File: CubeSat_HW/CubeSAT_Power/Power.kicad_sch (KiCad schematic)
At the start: 12 parts, among them J1 USB_B_Micro, J2 Conn_01x02_Pin, J4 Conn_02x20_Odd_Even, Q1 AO3401A, Q2 AO3401A, U1 LM1117MP-5.0

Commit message: feat: Added new version for the Power Supply Board
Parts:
- removed Q2: AO3401A, Package_TO_SOT_SMD:SOT-23, symbol Transistor_FET:AO3401A
- added D1: 12V, Diode_SMD:D_SOD-123, symbol Device:D_Zener
- added Q2: IRLML2502, Package_TO_SOT_SMD:SOT-23, symbol Transistor_FET:IRLZ44N
- added R1: 10k, Resistor_SMD:R_0603_1608Metric, symbol Device:R
- added R2: 10R, Resistor_SMD:R_0603_1608Metric, symbol Device:R
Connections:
- net COMMAND: now also R2.1
- net GND: now also D1.2 (A), Q2.3 (S), R1.2
- net VOut: now also Q2.2 (D)
- new net: D1.1 (K), Q2.1 (G), R1.1, R2.2

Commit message: fix: Minor fixes to the Power Supply Board
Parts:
- removed D1: 12V, Diode_SMD:D_SOD-123, symbol Device:D_Zener
- removed Q2: IRLML2502, Package_TO_SOT_SMD:SOT-23, symbol Transistor_FET:IRLZ44N
- added J6: Conn_02x20_Odd_Even, symbol Connector_Generic:Conn_02x20_Odd_Even
- added Q2: 2N7002, Package_TO_SOT_SMD:SOT-23, symbol Transistor_FET:2N7002
- added Q3: IRLM2502, Package_TO_SOT_SMD:SOT-23, symbol Transistor_FET:AO3401A
- added R3, R4, R5: 100k, Resistor_SMD:R_0603_1608Metric, symbol Device:R
- R1: value 10k -> 1k
- R2: value 10R -> 100k
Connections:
- net COMMAND: now also R1.2; no longer R2.1
- net GND: now also R2.2, Q2.2 (S), R3.1, R4.1; no longer R1.2
- net at R1.1: now also R2.1, Q2.1 (G); no longer R2.2
- net at J1.2 (D-): now also R4.2
- net at J1.3 (D+): now also R3.2
- net VOut: no longer names the net of C2.1, U1.2 (VO)
- net VOut: now also Q3.2 (S), R5.2; no longer J1.1 (VBUS)
- new net: Q2.3 (D), Q3.1 (G), R5.1
- new net: J1.1 (VBUS), Q3.3 (D)
- no-connect marks 3 -> 1
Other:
- moved on the sheet: J1

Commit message: release: Added version II of PS project.
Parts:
- removed J1: USB_B_Micro, Connector_USB:USB_Micro-B_GCT_USB3076-30-A, symbol Connector:USB_B_Micro
- added J3: USB_A, Connector_USB:USB_A_CNCTech_1001-011-01101_Horizontal, symbol Connector:USB_A
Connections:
- net GND: now also J3.4 (GND), J3.5 (Shield)
- net at R4.2: now also J3.2 (D-)
- net at R3.2: now also J3.3 (D+)
- net at Q3.3 (D): now also J3.1 (VBUS)
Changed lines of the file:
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@@
   (junction (at 77.724 23.241) (diameter 0) (color 0 0 0 0)
   )
+  (junction (at 24.13 72.136) (diameter 0) (color 0 0 0 0)
+  )
   (junction (at 66.548 34.925) (diameter 0) (color 0 0 0 0)
   )
   (junction (at 74.93 72.898) (diameter 0) (color 0 0 0 0)
-  )
-  (junction (at 24.638 72.136) (diameter 0) (color 0 0 0 0)
   )
   (junction (at 56.515 23.114) (diameter 0) (color 0 0 0 0)
@@
     (stroke (width 0) (type default))
   )
+  (wire (pts (xy 23.114 72.136) (xy 24.13 72.136))
+    (stroke (width 0) (type default))
+  )
   (wire (pts (xy 56.515 34.925) (xy 66.548 34.925))
     (stroke (width 0) (type default))
   )
-  (wire (pts (xy 24.638 72.136) (xy 24.638 74.422))
-    (stroke (width 0) (type default))
-  )
   (wire (pts (xy 56.515 23.114) (xy 50.292 23.114))
     (stroke (width 0) (type default))
@@
     (stroke (width 0) (type default))
   )
-  (wire (pts (xy 39.243 64.516) (xy 33.401 64.516))
+  (wire (pts (xy 33.274 64.516) (xy 39.243 64.516))
     (stroke (width 0) (type default))
   )
@@
     (stroke (width 0) (type default))
   )
-  (wire (pts (xy 23.241 72.136) (xy 24.638 72.136))
-    (stroke (width 0) (type default))
-  )
   (wire (pts (xy 227.33 33.655) (xy 246.888 33.655))
     (stroke (width 0) (type default))
@@
     (stroke (width 0) (type default))
   )
-  (wire (pts (xy 43.561 61.976) (xy 33.401 61.976))
+  (wire (pts (xy 33.274 61.976) (xy 43.561 61.976))
     (stroke (width 0) (type default))
   )
@@
     (stroke (width 0) (type default))
   )
+  (wire (pts (xy 24.13 72.136) (xy 24.13 74.168))
+    (stroke (width 0) (type default))
+  )
+  (wire (pts (xy 24.13 72.136) (xy 25.654 72.136))
+    (stroke (width 0) (type default))
+  )
   (wire (pts (xy 84.455 66.167) (xy 93.091 66.167))
     (stroke (width 0) (type default))
@@
     (stroke (width 0) (type default))
   )
-  (wire (pts (xy 24.638 72.136) (xy 25.781 72.136))
-    (stroke (width 0) (type default))
-  )
   (wire (pts (xy 28.067 23.114) (xy 40.132 23.114))
     (stroke (width 0) (type default))
@@
     (stroke (width 0) (type default))
   )
-  (wire (pts (xy 33.401 56.896) (xy 79.375 56.896))
+  (wire (pts (xy 33.274 56.896) (xy 79.375 56.896))
     (stroke (width 0) (type default))
   )
@@
       (effects (font (size 1.27 1.27)) hide)
     )
-    (pin "2")
-    (pin "1")
+    (pin "1")
+    (pin "2")
     (instances
       (project "Power"
@@
       (effects (font (size 1.27 1.27)) hide)
     )
-    (pin "2")
-    (pin "1")
+    (pin "1")
+    (pin "2")
     (instances
       (project "Power"
@@
       (effects (font (size 1.27 1.27)) hide)
     )
-    (pin "2")
-    (pin "1")
+    (pin "1")
+    (pin "2")
     (instances
       (project "Power"
@@
       (effects (font (size 1.27 1.27)) (justify left) hide)
     )
+    (pin "1")
     (pin "2")
     (pin "3")
-    (pin "1")
     (instances
       (project "Power"
@@
       (effects (font (size 1.27 1.27)) hide)
     )
-    (pin "2")
-    (pin "1")
+    (pin "1")
+    (pin "2")
     (instances
       (project "Power"
@@
         (path "/ac9d7e28-4551-4313-b6f7-b1e4cd4b0a31"
           (reference "#PWR04") (unit 1)
+        )
+      )
+    )
+  )
+  (symbol (lib_id "Connector:USB_A") (at 25.654 61.976 0) (unit 1)
+    (in_bom yes) (on_board yes) (dnp no) (fields_autoplaced)
+    (property "Reference" "J3" (at 25.654 49.276 0)
+      (effects (font (size 1.27 1.27)))
+    )
+    (property "Value" "USB_A" (at 25.654 51.816 0)
+      (effects (font (size 1.27 1.27)))
+    )
+    (property "Footprint" "Connector_USB:USB_A_CNCTech_1001-011-01101_Horizontal" (at 29.464 63.246 0)
+      (effects (font (size 1.27 1.27)) hide)
+    )
+    (property "Datasheet" " ~" (at 29.464 63.246 0)
+      (effects (font (size 1.27 1.27)) hide)
+    )
+    (pin "1")
+    (pin "2")
+    (pin "3")
+    (pin "4")
+    (pin "5")
+    (instances
+      (project "Power"
+        (path "/ac9d7e28-4551-4313-b6f7-b1e4cd4b0a31"
+          (reference "J3") (unit 1)
         )
       )
@@
       (effects (font (size 1.27 1.27)) hide)
     )
+    (pin "1")
+    (pin "10")
+    (pin "11")
     (pin "12")
     (pin "13")
-    (pin "20")
-    (pin "23")
-    (pin "19")
-    (pin "24")
-    (pin "27")
-    (pin "3")
+    (pin "14")
+    (pin "15")
+    (pin "16")
     (pin "17")
     (pin "18")
-    (pin "2")
+    (pin "19")
+    (pin "2")
+    (pin "20")
     (pin "21")
+    (pin "22")
+    (pin "23")
+    (pin "24")
     (pin "25")
-    (pin "1")
-    (pin "15")
-    (pin "11")
-    (pin "14")
     (pin "26")
+    (pin "27")
+    (pin "28")
     (pin "29")
-    (pin "10")
+    (pin "3")
     (pin "30")
-    (pin "22")
-    (pin "28")
-    (pin "16")
+    (pin "31")
     (pin "32")
+    (pin "33")
+    (pin "34")
+    (pin "35")
     (pin "36")
-    (pin "35")
+    (pin "37")
     (pin "38")
     (pin "39")
+    (pin "4")
     (pin "40")
-    (pin "37")
     (pin "5")
-    (pin "34")
+    (pin "6")
+    (pin "7")
+    (pin "8")
     (pin "9")
-    (pin "4")
-    (pin "31")
-    (pin "7")
-    (pin "33")
-    (pin "8")
-    (pin "6")
     (instances
       (project "Power"
@@
     )
     (pin "1")
+    (pin "2")
     (pin "3")
-    (pin "2")
     (instances
       (project "Power"
@@
       (effects (font (size 1.27 1.27)) hide)
     )
+    (pin "1")
+    (pin "2")
     (pin "3")
-    (pin "1")
-    (pin "2")
     (instances
       (project "Power"
@@
       (effects (font (size 1.27 1.27)) hide)
     )
-    (pin "2")
-    (pin "1")
+    (pin "1")
+    (pin "2")
     (instances
       (project "Power"
@@
     )
   )
-  (symbol (lib_id "power:GND") (at 24.638 74.422 0) (unit 1)
-    (in_bom yes) (on_board yes) (dnp no) (fields_autoplaced)
-    (property "Reference" "#PWR01" (at 24.638 80.772 0)
-      (effects (font (size 1.27 1.27)) hide)
-    )
-    (property "Value" "GND" (at 24.638 79.248 0)
-      (effects (font (size 1.27 1.27)))
-    )
-    (property "Footprint" "" (at 24.638 74.422 0)
-      (effects (font (size 1.27 1.27)) hide)
-    )
-    (property "Datasheet" "" (at 24.638 74.422 0)
+  (symbol (lib_id "power:GND") (at 24.13 74.168 0) (unit 1)
+    (in_bom yes) (on_board yes) (dnp no) (fields_autoplaced)
+    (property "Reference" "#PWR01" (at 24.13 80.518 0)
+      (effects (font (size 1.27 1.27)) hide)
+    )
+    (property "Value" "GND" (at 24.13 78.994 0)
+      (effects (font (size 1.27 1.27)))
+    )
+    (property "Footprint" "" (at 24.13 74.168 0)
+      (effects (font (size 1.27 1.27)) hide)
+    )
+    (property "Datasheet" "" (at 24.13 74.168 0)
       (effects (font (size 1.27 1.27)) hide)
     )
@@
         (path "/ac9d7e28-4551-4313-b6f7-b1e4cd4b0a31"
           (reference "#PWR05") (unit 1)
-        )
-      )
-    )
-  )
-  (symbol (lib_id "Connector:USB_B_Micro") (at 25.781 61.976 0) (unit 1)
-    (in_bom yes) (on_board yes) (dnp no) (fields_autoplaced)
-    (property "Reference" "J1" (at 25.781 50.038 0)
-      (effects (font (size 1.27 1.27)))
-    )
-    (property "Value" "USB_B_Micro" (at 25.781 52.578 0)
-      (effects (font (size 1.27 1.27)) hide)
-    )
-    (property "Footprint" "Connector_USB:USB_Micro-B_GCT_USB3076-30-A" (at 29.591 63.246 0)
-      (effects (font (size 1.27 1.27)) hide)
-    )
-    (property "Datasheet" "~" (at 29.591 63.246 0)
-      (effects (font (size 1.27 1.27)) hide)
-    )
-    (pin "1")
-    (pin "2")
-    (pin "3")
-    (pin "4")
-    (pin "5")
-    (pin "6")
-    (instances
-      (project "Power"
-        (path "/ac9d7e28-4551-4313-b6f7-b1e4cd4b0a31"
-          (reference "J1") (unit 1)
         )
       )
@@
       (effects (font (size 1.27 1.27)) (justify left) hide)
     )
+    (pin "1")
     (pin "2")
     (pin "3")
-    (pin "1")
-    (instances
-      (project "Power"
+    (instances
+      (project "Power"

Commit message: fix: Small changes
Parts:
- removed J3: USB_A, Connector_USB:USB_A_CNCTech_1001-011-01101_Horizontal, symbol Connector:USB_A
- removed J4: Conn_02x20_Odd_Even, Connector_PinHeader_2.54mm:PinHeader_2x20_P2.54mm_Vertical, symbol Connector_Generic:Conn_02x20_Odd_Even
- removed J6: Conn_02x20_Odd_Even, symbol Connector_Generic:Conn_02x20_Odd_Even
- added J1: USB_B_Micro, Connector_USB:USB_Micro-B_GCT_USB3076-30-A, symbol Connector:USB_B_Micro
- added J3: Conn_02x17_Odd_Even, Connector_IDC:IDC-Header_2x17_P2.54mm_Horizontal, symbol Connector_Generic:Conn_02x17_Odd_Even
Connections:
- net COMMAND: now also J3.33 (Pin_33), J3.34 (Pin_34)
- net GND: now also J1.5 (GND), J1.6 (Shield), J3.3 (Pin_3), J3.4 (Pin_4)
- net at R4.2: now also J1.2 (D-)
- net at R3.2: now also J1.3 (D+)
- net at Q3.3 (D): now also J1.1 (VBUS)
- new net +3.3V: J3.1 (Pin_1), J3.2 (Pin_2)
- new net CE: J3.17 (Pin_17), J3.18 (Pin_18)
- new net CSN: J3.15 (Pin_15), J3.16 (Pin_16)
- new net LED3: J3.23 (Pin_23), J3.24 (Pin_24)
- new net LED4: J3.25 (Pin_25), J3.26 (Pin_26)
- new net LED5: J3.27 (Pin_27), J3.28 (Pin_28)
- new net LED_1: J3.19 (Pin_19), J3.20 (Pin_20)
- new net LED_2: J3.21 (Pin_21), J3.22 (Pin_22)
- new net MISO: J3.11 (Pin_11), J3.12 (Pin_12)
- new net MOSI: J3.10 (Pin_10), J3.9 (Pin_9)
- new net PWM0: J3.29 (Pin_29), J3.30 (Pin_30)
- new net PWM1: J3.31 (Pin_31), J3.32 (Pin_32)
- new net SCK: J3.13 (Pin_13), J3.14 (Pin_14)
- new net SCL: J3.7 (Pin_7), J3.8 (Pin_8)
- new net SDA: J3.5 (Pin_5), J3.6 (Pin_6)

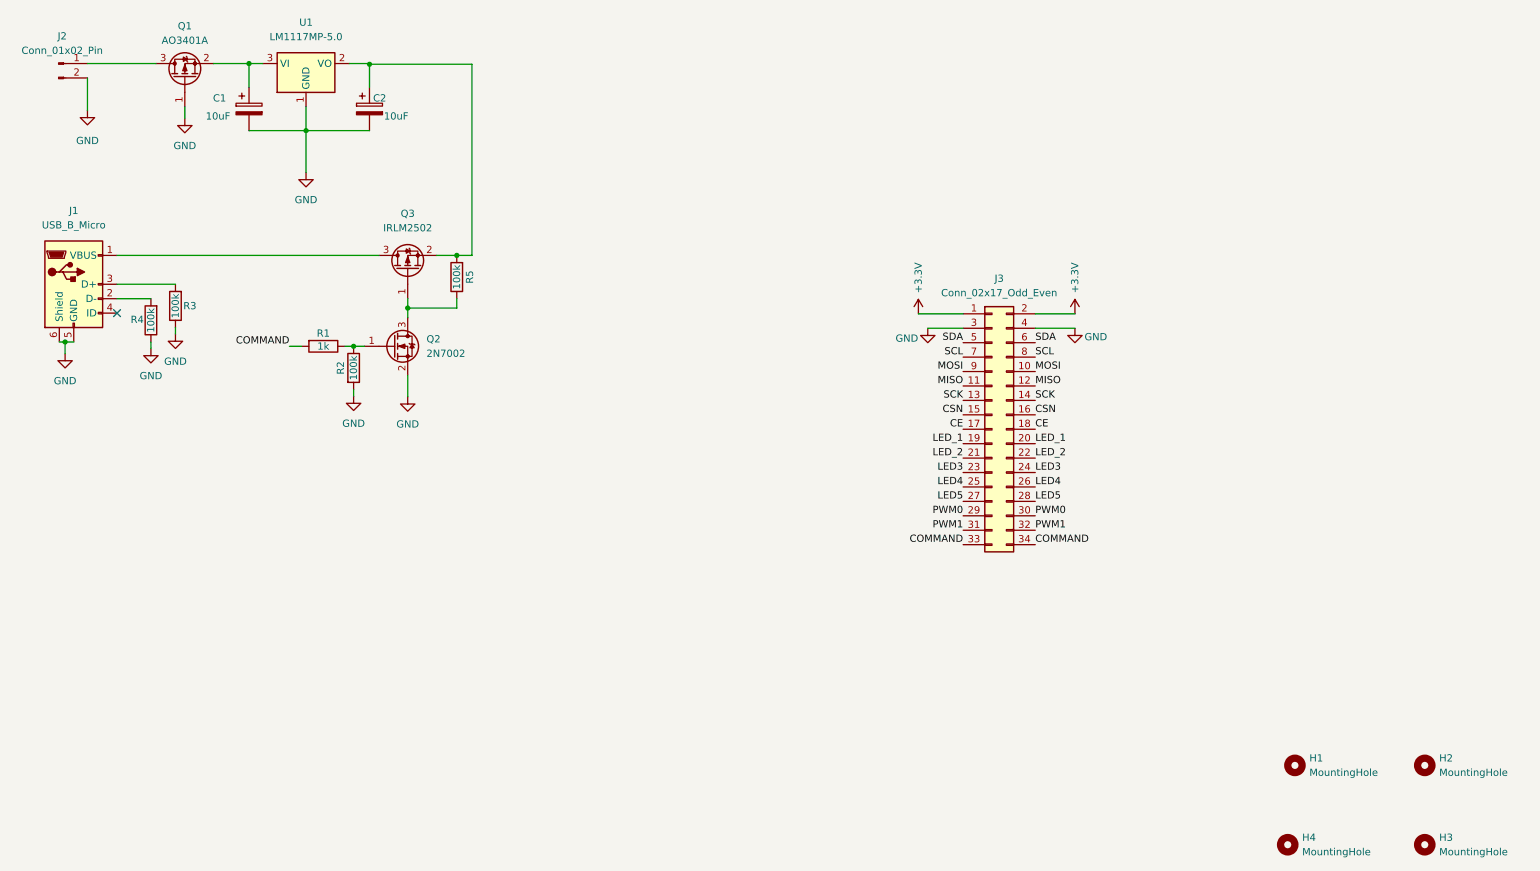
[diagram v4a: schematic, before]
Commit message: feat: Added Payload Board and new Gerbers for the project
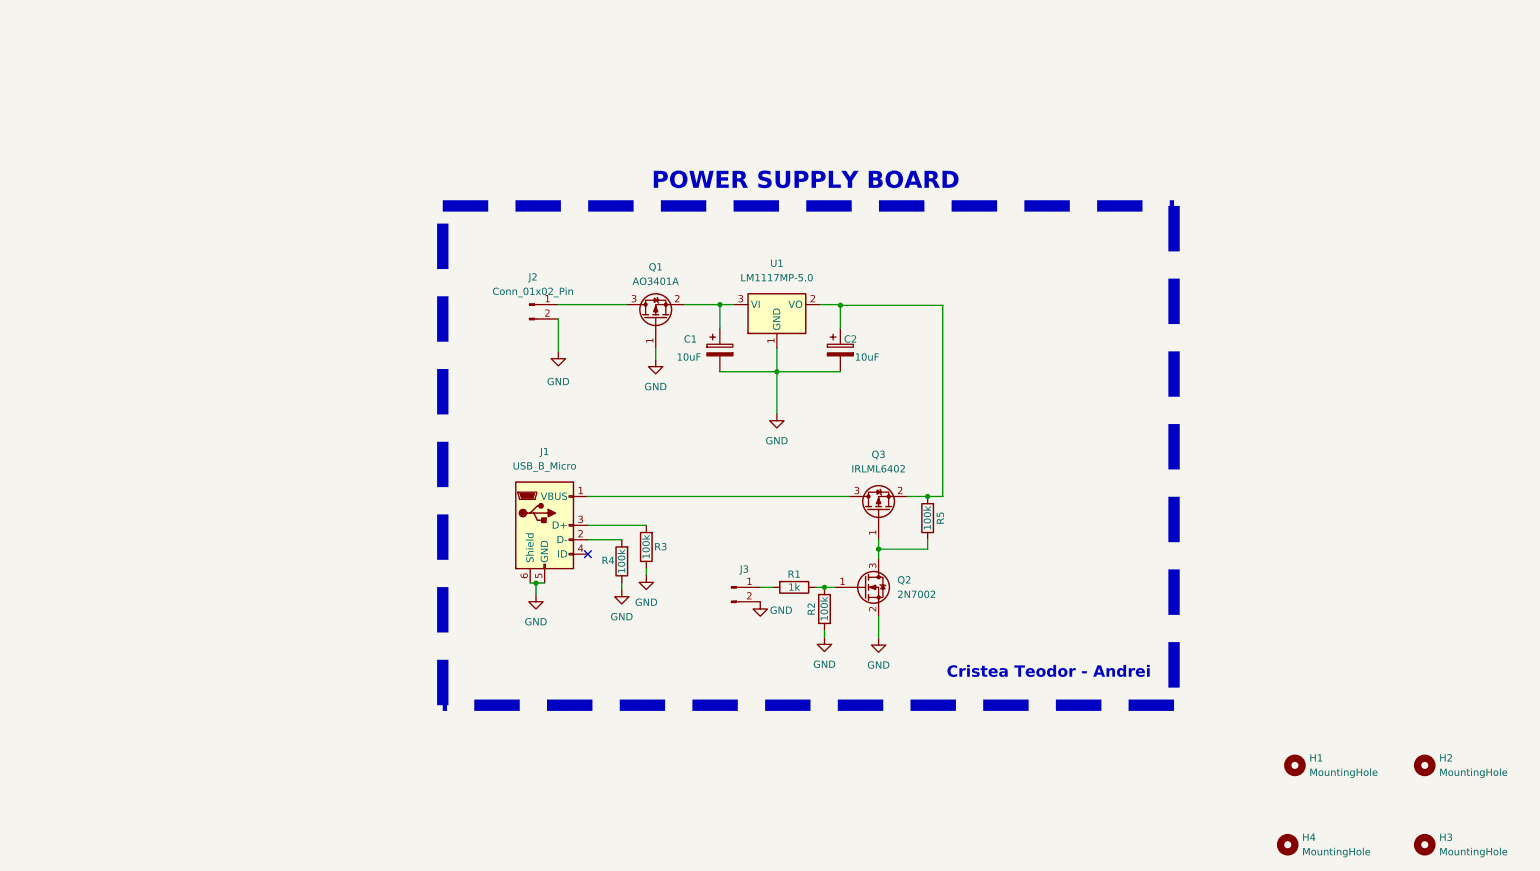
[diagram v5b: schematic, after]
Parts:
- removed J3: Conn_02x17_Odd_Even, Connector_IDC:IDC-Header_2x17_P2.54mm_Horizontal, symbol Connector_Generic:Conn_02x17_Odd_Even
- added J3: Conn_01x02_Pin, Connector_PinHeader_2.54mm:PinHeader_1x02_P2.54mm_Vertical, symbol Connector:Conn_01x02_Pin
- J2: footprint Connector_TE-Connectivity:TE_440055-2_1x02_P2.00mm_Horizontal -> Connector_PinHeader_2.54mm:PinHeader_1x02_P2.54mm_Vertical
- Q3: value IRLM2502 -> IRLML6402
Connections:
- net GND: now also J3.2 (Pin_2)
- net COMMAND: no longer names the net of R1.2
- net COMMAND: now also J3.1 (Pin_1)
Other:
- note added: "Cristea Teodor - Andrei"
- note added: "POWER SUPPLY BOARD"
- moved on the sheet: C1, C2, J1, J2, Q1, Q2, Q3, R1, R2, R3, R4, R5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
